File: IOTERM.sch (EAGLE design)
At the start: 45 parts

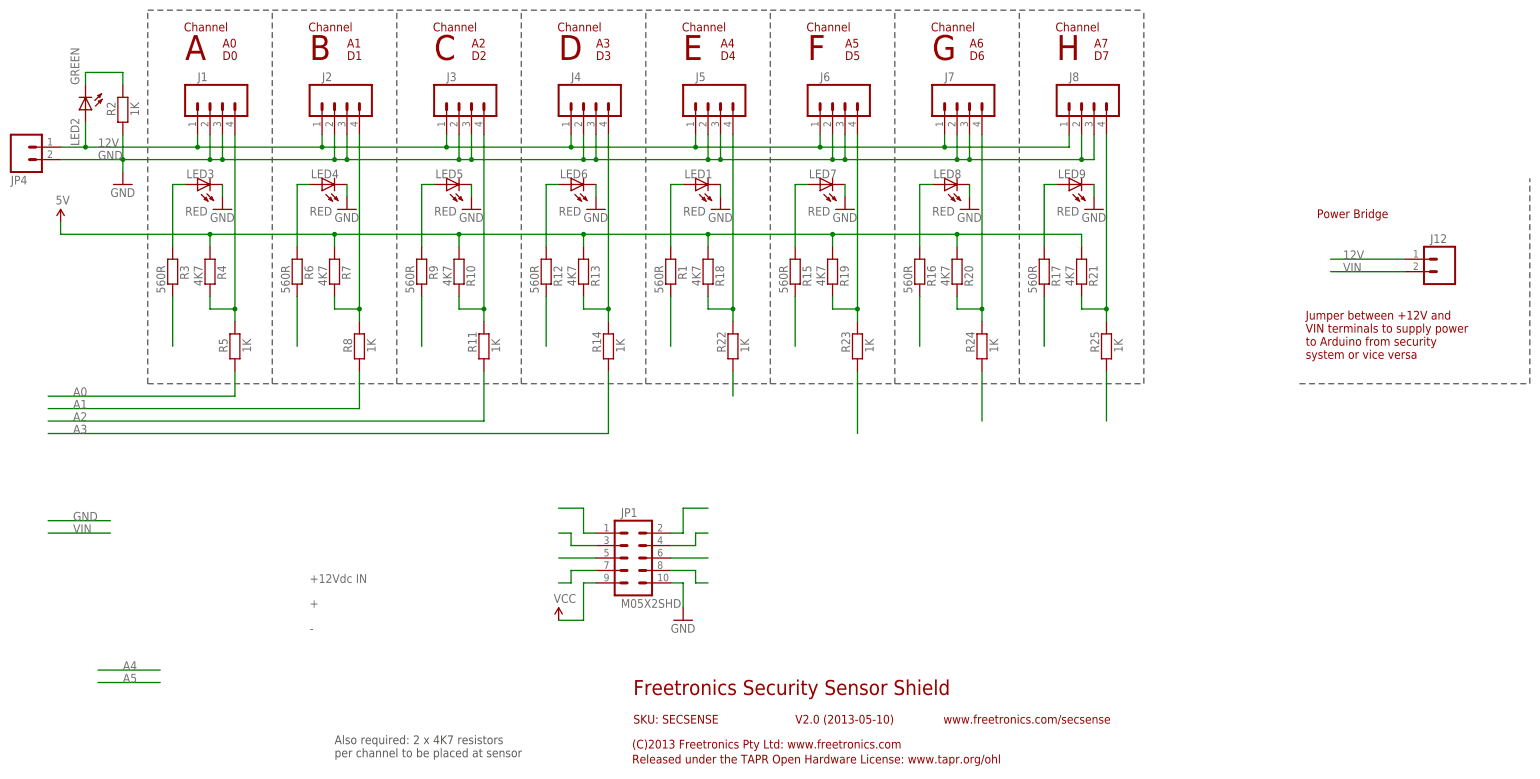
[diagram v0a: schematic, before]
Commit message: Expanded header to 2x6 for v2.0 release
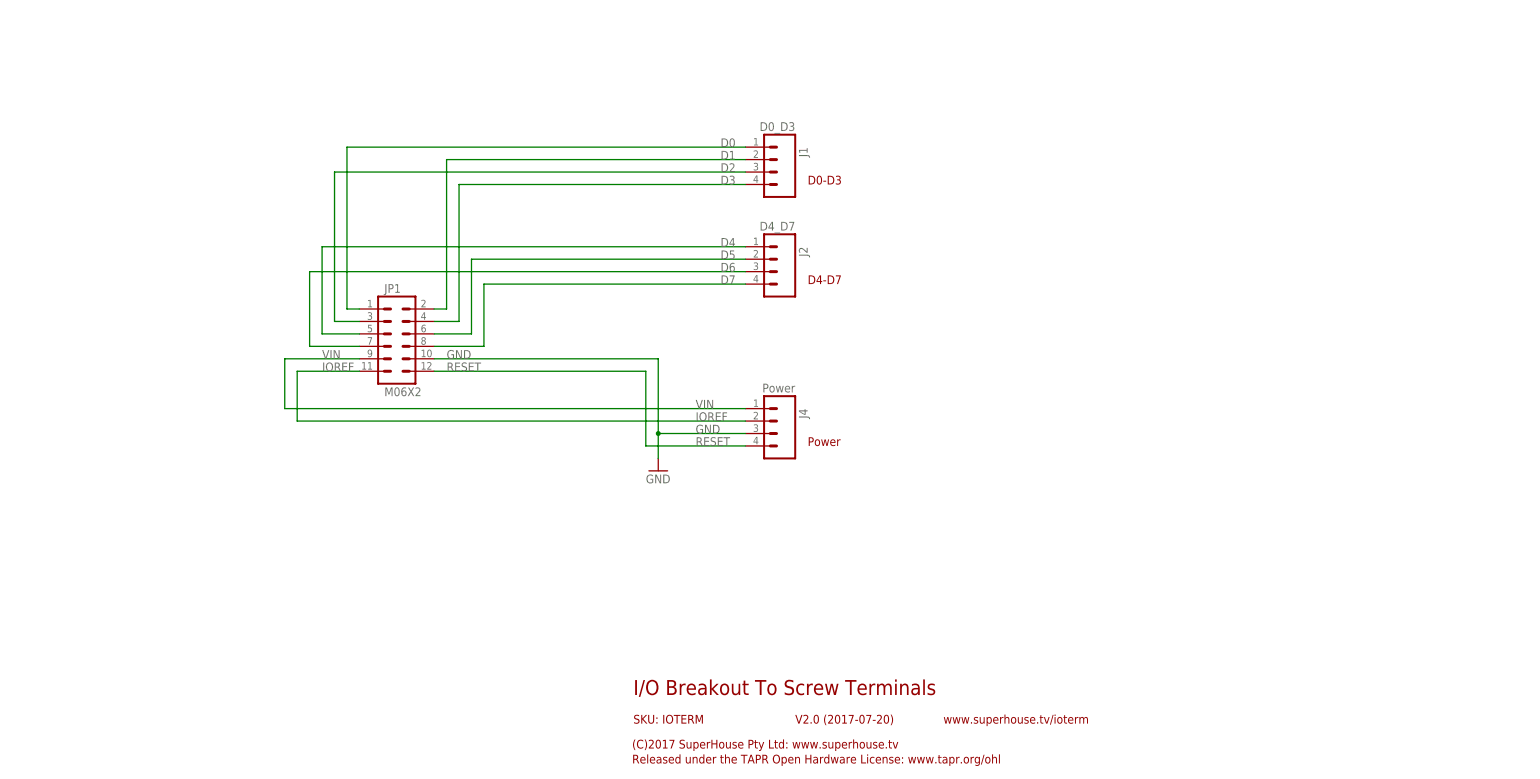
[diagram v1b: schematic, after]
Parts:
- removed J12: (no value), freetronics-original:M02PTH
- removed J3, J5, J6, J7, J8: (no value), freetronics-master-v1.1:M04SCREW
- removed JP4: (no value), freetronics-master-v1.1:M023.5MM
- removed LED1, LED3, LED4, LED5, LED6, LED7, LED8, LED9: RED, freetronics-jon:LED0603
- removed LED2: GREEN, freetronics-jon:LED0603
- removed R1, R12, R15, R16, R17, R3, R6, R9: 560R, freetronics-jon:RESISTOR0603
- removed R10, R13, R18, R19, R20, R21, R4, R7: 4K7, freetronics-jon:RESISTOR0603
- removed R11, R14, R2, R22, R23, R24, R25, R5, R8: 1K, freetronics-jon:RESISTOR0603
- J1: value (none) -> D0_D3
- J2: value (none) -> D4_D7
- J4: value (none) -> Power
- JP1: value M05X2SHD -> M06X2; device freetronics-original:M05X2SHD -> freetronics-jon:M06X2
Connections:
- removed net 12V: J1.1, J12.1, J2.1, J3.1, J4.1, J5.1, J6.1, J7.1, J8.1, JP4.1, LED2.A
- removed net 5V: R10.1, R13.1, R18.1, R19.1, R20.1, R21.1, R4.1, R7.1
- removed net A0: R5.1
- removed net A1: R8.1
- removed net A2: R11.1
- removed net A3: R14.1
- removed net N$1: LED2.C, R2.2
- removed net N$10: J8.4, R21.2, R25.2
- removed net N$11: JP1.5
- removed net N$12: JP1.3
- removed net N$13: JP1.1
- removed net N$14: JP1.7
- removed net N$15: LED1.A, R1.1
- removed net N$16: LED7.A, R15.1
- removed net N$17: LED8.A, R16.1
- removed net N$18: LED9.A, R17.1
- removed net N$19: R1.2
- removed net N$2: R3.2
- removed net N$20: R15.2
- removed net N$21: R16.2
- removed net N$22: R17.2
- removed net N$23: R22.1
- removed net N$24: R23.1
- removed net N$249: J3.4, R10.2, R11.2
- removed net N$25: R24.1
- removed net N$251: LED6.A, R12.1
- removed net N$252: LED5.A, R9.1
- removed net N$253: LED4.A, R6.1
- removed net N$254: LED3.A, R3.1
- removed net N$256: J4.4, R13.2, R14.2
- removed net N$26: R25.1
- removed net N$262: J1.4, R4.2, R5.2
- removed net N$27: JP1.8
- removed net N$28: JP1.6
- removed net N$29: JP1.4
- removed net N$3: J2.4, R7.2, R8.2
- removed net N$30: JP1.2
- removed net N$4: R6.2
- removed net N$5: R9.2
- removed net N$6: R12.2
- removed net N$7: J5.4, R18.2, R22.2
- removed net N$8: J6.4, R19.2, R23.2
- removed net N$9: J7.4, R20.2, R24.2
- removed net VCC: JP1.9
- new net D0: J1.1, JP1.1
- new net D1: J1.2, JP1.2
- new net D2: J1.3, JP1.3
- new net D3: J1.4, JP1.4
- new net D4: J2.1, JP1.5
- new net D5: J2.2, JP1.6
- new net D6: J2.3, JP1.7
- new net D7: J2.4, JP1.8
- new net IOREF: J4.2, JP1.11
- new net RESET: J4.4, JP1.12
- net GND: no longer J1.2, J1.3, J2.2, J2.3, J3.2, J3.3, J4.2, J5.2, J5.3, J6.2, J6.3, J7.2, J7.3, J8.2, J8.3, JP4.2, LED1.C, LED3.C, LED4.C, LED5.C, LED6.C, LED7.C, LED8.C, LED9.C, R2.1
- net VIN: now also J4.1, JP1.9; no longer J12.2
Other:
- note added: "(C)2017 SuperHouse Pty Ltd: www.superhouse.tv"
- note added: "D0-D3"
- note added: "D4-D7"
- note added: "I/O Breakout To Screw Terminals"
- note added: "Power"
- note added: "SKU: IOTERM"
- note added: "V2.0 (2017-07-20)"
- note added: "www.superhouse.tv/ioterm"
- note removed: "(C)2013 Freetronics Pty Ltd: www.freetronics.com"
- note removed: "+"
- note removed: "+12Vdc IN"
- note removed: "-"
- note removed: "A"
- note removed: "A0"
- note removed: "A1"
- note removed: "A2"
- note removed: "A3"
- note removed: "A4"
- note removed: "A5"
- note removed: "A6"
- note removed: "A7"
- note removed: "Also required: 2 x 4K7 resistors per channel to be placed at sensor"
- note removed: "B"
- note removed: "C"
- note removed: "Channel"
- note removed: "D"
- note removed: "D0"
- note removed: "D1"
- note removed: "D2"
- note removed: "D3"
- note removed: "D4"
- note removed: "D5"
- note removed: "D6"
- note removed: "D7"
- note removed: "E"
- note removed: "F"
- note removed: "Freetronics Security Sensor Shield"
- note removed: "G"
- note removed: "H"
- note removed: "Jumper between +12V and VIN terminals to supply power to Arduino from security system or vice versa"
- note removed: "Power Bridge"
- note removed: "SKU: SECSENSE"
- note removed: "V2.0 (2013-05-10)"
- note removed: "www.freetronics.com/secsense"
- moved on the sheet: J1, J2, J4

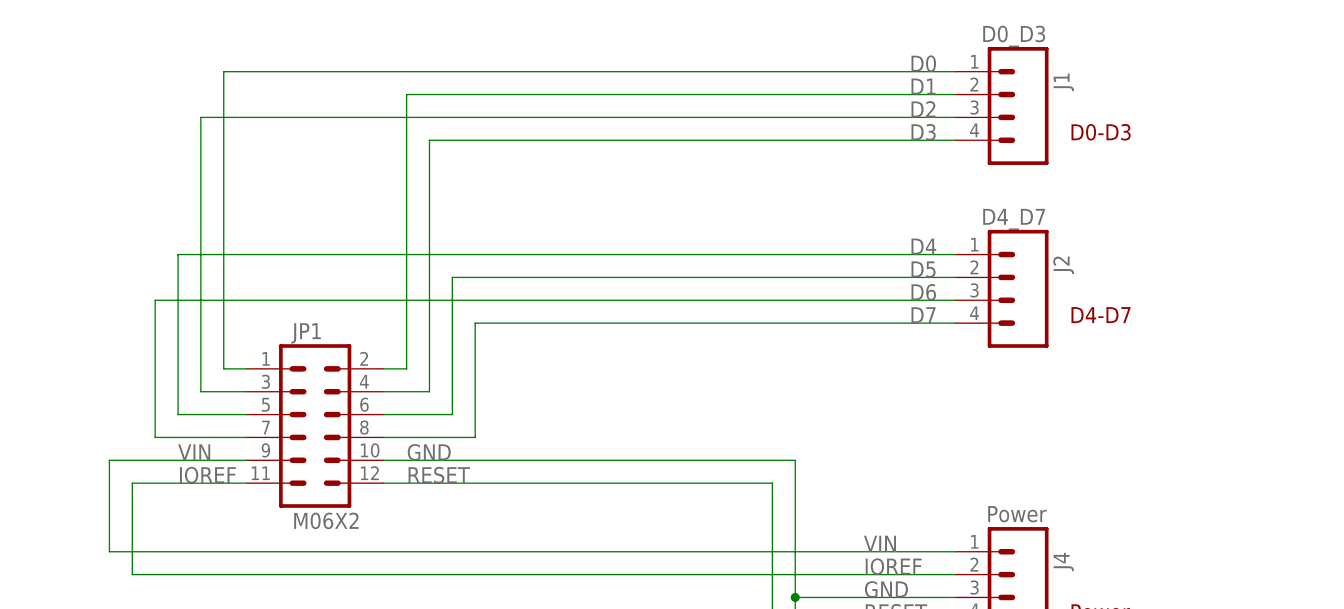
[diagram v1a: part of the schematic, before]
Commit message: Adjusted size to metric grid
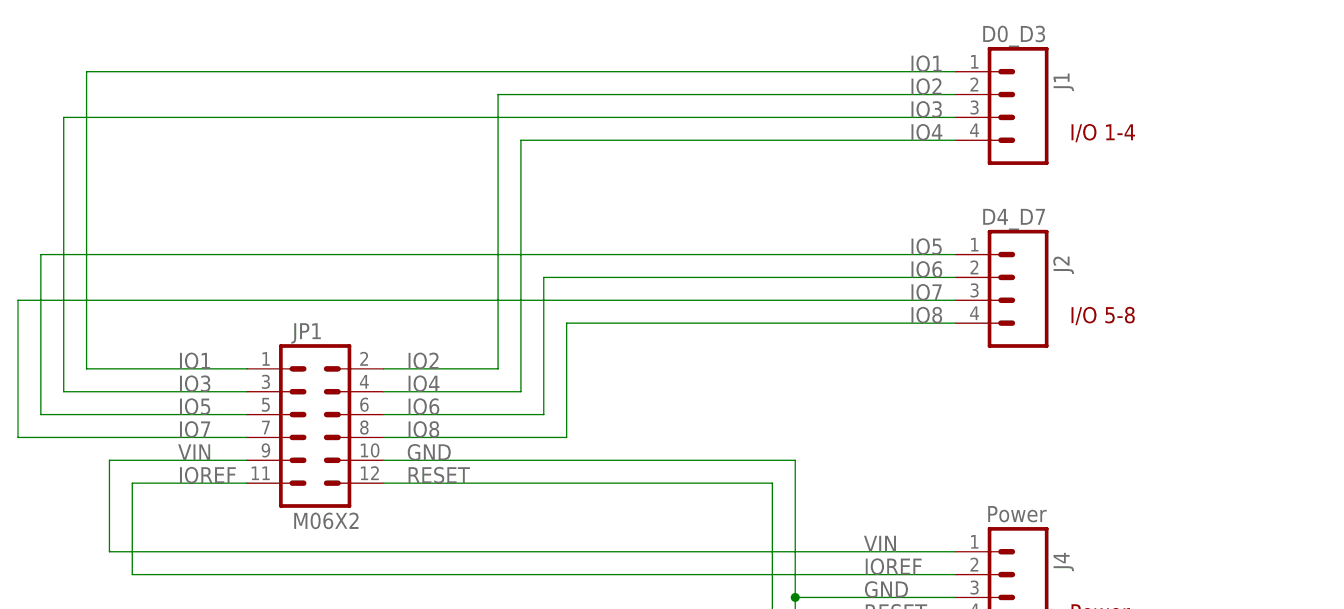
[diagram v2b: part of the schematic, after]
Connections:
- net D0 renamed IO1
- net D1 renamed IO2
- net D2 renamed IO3
- net D3 renamed IO4
- net D4 renamed IO5
- net D5 renamed IO6
- net D6 renamed IO7
- net D7 renamed IO8
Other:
- note added: "I/O 1-4"
- note added: "I/O 5-8"
- note removed: "D0-D3"
- note removed: "D4-D7"
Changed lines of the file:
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@@
 <sheet>
 <plain>
-<text x="170.18" y="124.46" size="1.778" layer="94">D0-D3</text>
-<text x="170.18" y="104.14" size="1.778" layer="94">D4-D7</text>
+<text x="170.18" y="124.46" size="1.778" layer="94">I/O 1-4</text>
+<text x="170.18" y="104.14" size="1.778" layer="94">I/O 5-8</text>
 <frame x1="0" y1="0" x2="248.92" y2="185.42" columns="8" rows="5" layer="94"/>
 <text x="134.62" y="20.32" size="3.048" layer="94">I/O Breakout To Screw Terminals</text>
@@
 </segment>
 </net>
-<net name="D4" class="0">
+<net name="IO5" class="0">
 <segment>
 <pinref part="JP1" gate="G$1" pin="5"/>
-<wire x1="71.12" y1="93.98" x2="78.74" y2="93.98" width="0.1524" layer="91"/>
-<wire x1="71.12" y1="93.98" x2="71.12" y2="111.76" width="0.1524" layer="91"/>
+<wire x1="55.88" y1="93.98" x2="78.74" y2="93.98" width="0.1524" layer="91"/>
+<wire x1="55.88" y1="93.98" x2="55.88" y2="111.76" width="0.1524" layer="91"/>
 <pinref part="J2" gate="G$1" pin="1"/>
-<wire x1="71.12" y1="111.76" x2="157.48" y2="111.76" width="0.1524" layer="91"/>
+<wire x1="55.88" y1="111.76" x2="157.48" y2="111.76" width="0.1524" layer="91"/>
 <label x="152.4" y="111.76" size="1.778" layer="95"/>
+<label x="71.12" y="93.98" size="1.778" layer="95"/>
 </segment>
 </net>
-<net name="D2" class="0">
+<net name="IO3" class="0">
 <segment>
 <pinref part="JP1" gate="G$1" pin="3"/>
-<wire x1="78.74" y1="96.52" x2="73.66" y2="96.52" width="0.1524" layer="91"/>
-<wire x1="73.66" y1="96.52" x2="73.66" y2="127" width="0.1524" layer="91"/>
+<wire x1="78.74" y1="96.52" x2="58.42" y2="96.52" width="0.1524" layer="91"/>
+<wire x1="58.42" y1="96.52" x2="58.42" y2="127" width="0.1524" layer="91"/>
 <pinref part="J1" gate="G$1" pin="3"/>
-<wire x1="73.66" y1="127" x2="157.48" y2="127" width="0.1524" layer="91"/>
+<wire x1="58.42" y1="127" x2="157.48" y2="127" width="0.1524" layer="91"/>
 <label x="152.4" y="127" size="1.778" layer="95"/>
+<label x="71.12" y="96.52" size="1.778" layer="95"/>
 </segment>
 </net>
-<net name="D0" class="0">
+<net name="IO1" class="0">
 <segment>
 <pinref part="JP1" gate="G$1" pin="1"/>
-<wire x1="78.74" y1="99.06" x2="76.2" y2="99.06" width="0.1524" layer="91"/>
-<wire x1="76.2" y1="99.06" x2="76.2" y2="132.08" width="0.1524" layer="91"/>
+<wire x1="78.74" y1="99.06" x2="60.96" y2="99.06" width="0.1524" layer="91"/>
+<wire x1="60.96" y1="99.06" x2="60.96" y2="132.08" width="0.1524" layer="91"/>
 <pinref part="J1" gate="G$1" pin="1"/>
-<wire x1="76.2" y1="132.08" x2="157.48" y2="132.08" width="0.1524" layer="91"/>
+<wire x1="60.96" y1="132.08" x2="157.48" y2="132.08" width="0.1524" layer="91"/>
 <label x="152.4" y="132.08" size="1.778" layer="95"/>
+<label x="71.12" y="99.06" size="1.778" layer="95"/>
 </segment>
 </net>
-<net name="D6" class="0">
+<net name="IO7" class="0">
 <segment>
 <pinref part="JP1" gate="G$1" pin="7"/>
-<wire x1="78.74" y1="91.44" x2="68.58" y2="91.44" width="0.1524" layer="91"/>
-<wire x1="68.58" y1="91.44" x2="68.58" y2="106.68" width="0.1524" layer="91"/>
+<wire x1="78.74" y1="91.44" x2="53.34" y2="91.44" width="0.1524" layer="91"/>
+<wire x1="53.34" y1="91.44" x2="53.34" y2="106.68" width="0.1524" layer="91"/>
 <pinref part="J2" gate="G$1" pin="3"/>
-<wire x1="68.58" y1="106.68" x2="157.48" y2="106.68" width="0.1524" layer="91"/>
+<wire x1="53.34" y1="106.68" x2="157.48" y2="106.68" width="0.1524" layer="91"/>
 <label x="152.4" y="106.68" size="1.778" layer="95"/>
+<label x="71.12" y="91.44" size="1.778" layer="95"/>
 </segment>
 </net>
-<net name="D7" class="0">
+<net name="IO8" class="0">
 <segment>
 <pinref part="JP1" gate="G$1" pin="8"/>
-<wire x1="93.98" y1="91.44" x2="104.14" y2="91.44" width="0.1524" layer="91"/>
-<wire x1="104.14" y1="91.44" x2="104.14" y2="104.14" width="0.1524" layer="91"/>
+<wire x1="93.98" y1="91.44" x2="114.3" y2="91.44" width="0.1524" layer="91"/>
+<wire x1="114.3" y1="91.44" x2="114.3" y2="104.14" width="0.1524" layer="91"/>
 <pinref part="J2" gate="G$1" pin="4"/>
-<wire x1="104.14" y1="104.14" x2="157.48" y2="104.14" width="0.1524" layer="91"/>
+<wire x1="114.3" y1="104.14" x2="157.48" y2="104.14" width="0.1524" layer="91"/>
 <label x="152.4" y="104.14" size="1.778" layer="95"/>
+<label x="96.52" y="91.44" size="1.778" layer="95"/>
 </segment>
 </net>
-<net name="D5" class="0">
+<net name="IO6" class="0">
 <segment>
 <pinref part="JP1" gate="G$1" pin="6"/>
-<wire x1="93.98" y1="93.98" x2="101.6" y2="93.98" width="0.1524" layer="91"/>
-<wire x1="101.6" y1="93.98" x2="101.6" y2="109.22" width="0.1524" layer="91"/>
+<wire x1="93.98" y1="93.98" x2="111.76" y2="93.98" width="0.1524" layer="91"/>
+<wire x1="111.76" y1="93.98" x2="111.76" y2="109.22" width="0.1524" layer="91"/>
 <pinref part="J2" gate="G$1" pin="2"/>
-<wire x1="101.6" y1="109.22" x2="157.48" y2="109.22" width="0.1524" layer="91"/>
+<wire x1="111.76" y1="109.22" x2="157.48" y2="109.22" width="0.1524" layer="91"/>
 <label x="152.4" y="109.22" size="1.778" layer="95"/>
+<label x="96.52" y="93.98" size="1.778" layer="95"/>
 </segment>
 </net>
-<net name="D3" class="0">
+<net name="IO4" class="0">
 <segment>
 <pinref part="JP1" gate="G$1" pin="4"/>
-<wire x1="93.98" y1="96.52" x2="99.06" y2="96.52" width="0.1524" layer="91"/>
-<wire x1="99.06" y1="96.52" x2="99.06" y2="124.46" width="0.1524" layer="91"/>
+<wire x1="93.98" y1="96.52" x2="109.22" y2="96.52" width="0.1524" layer="91"/>
+<wire x1="109.22" y1="96.52" x2="109.22" y2="124.46" width="0.1524" layer="91"/>
 <pinref part="J1" gate="G$1" pin="4"/>
-<wire x1="99.06" y1="124.46" x2="157.48" y2="124.46" width="0.1524" layer="91"/>
+<wire x1="109.22" y1="124.46" x2="157.48" y2="124.46" width="0.1524" layer="91"/>
 <label x="152.4" y="124.46" size="1.778" layer="95"/>
+<label x="96.52" y="96.52" size="1.778" layer="95"/>
 </segment>
 </net>
-<net name="D1" class="0">
+<net name="IO2" class="0">
 <segment>
 <pinref part="JP1" gate="G$1" pin="2"/>
-<wire x1="93.98" y1="99.06" x2="96.52" y2="99.06" width="0.1524" layer="91"/>
-<wire x1="96.52" y1="99.06" x2="96.52" y2="129.54" width="0.1524" layer="91"/>
+<wire x1="93.98" y1="99.06" x2="106.68" y2="99.06" width="0.1524" layer="91"/>
+<wire x1="106.68" y1="99.06" x2="106.68" y2="129.54" width="0.1524" layer="91"/>
 <pinref part="J1" gate="G$1" pin="2"/>
-<wire x1="96.52" y1="129.54" x2="157.48" y2="129.54" width="0.1524" layer="91"/>
+<wire x1="106.68" y1="129.54" x2="157.48" y2="129.54" width="0.1524" layer="91"/>
 <label x="152.4" y="129.54" size="1.778" layer="95"/>
+<label x="96.52" y="99.06" size="1.778" layer="95"/>
 </segment>
 </net>
